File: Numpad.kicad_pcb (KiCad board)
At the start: 2 copper layers, 119.9 x 104.8 mm, 50 parts, among them SW1 SW_Push, U1 ATmega32U4-AU, Y1 16MHz

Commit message: Commit all files before starting from scratch
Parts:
- C1, C2, C3, C4, C5, C6, C7, D1, D10, D11, D12, D13, D14, D15, D16, D17, D2, D3, D4, D5, D6, D7, D8, D9, F1, R1, R2, R3, R4, SW1, U1, USB1, Y1: moved to B.Cu
- moved SW1 66.5 mm to (68.3, 43.3), turned to 180 degrees
- moved R1 56.4 mm to (75.2, 43.3), turned to 180 degrees
- moved C5 44.0 mm to (80.8, 38.9), turned to 180 degrees
- moved F1 39.1 mm to (79.2, 34.5)
- moved C6 38.2 mm to (80.8, 44.2)
- moved C7 34.9 mm to (94.7, 35.6), turned to 0 degrees
- moved R3 31.2 mm to (79.7, 29.9)
- moved U1 30.1 mm to (90.2, 43.4), turned to 270 degrees
- moved C4 29.1 mm to (95.2, 53.8), turned to 0 degrees
- moved USB1 28.3 mm to (81.3, 20.8)
- moved C3 28.0 mm to (98.8, 34.0)
- moved R2 26.6 mm to (82.1, 29.9)
- moved R4 24.3 mm to (86.4, 52.3)
- moved Y1 21.1 mm to (102.9, 42.4), turned to 270 degrees
- moved C2 18.6 mm to (102.9, 38.9), turned to 180 degrees
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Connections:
- net Net-(R2-Pad1) renamed /USB_D+
- net Net-(R3-Pad1) renamed /USB_D-
- USB1 pad 5: Net-(USB1-Pad5) -> VCC
- USB1 pad 6: VCC -> Net-(USB1-Pad6)
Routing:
- net COL0: track 0.00 -> 169.8 mm, vias 0 -> 2
- net COL2: track 0.00 -> 115.8 mm, vias 0 -> 1
- net COL1: track 0.00 -> 114.5 mm, vias 0 -> 1
- net ROW3: track 0.00 -> 106.1 mm, vias 0 -> 2
- net ROW4: track 0.00 -> 102.2 mm, vias 0 -> 2
- net ROW0: track 0.00 -> 82.8 mm, vias 0 -> 6
- net COL3: track 0.00 -> 82.6 mm
- net ROW2: track 0.00 -> 72.6 mm, vias 0 -> 2
- net +5V: track 0.00 -> 68.7 mm
- net ROW1: track 0.00 -> 59.5 mm
- net Net-(R1-Pad2): track 0.00 -> 26.9 mm, vias 0 -> 2
- net /USB_D-: track 0.00 -> 11.6 mm
- net Net-(C2-Pad1): track 0.00 -> 11.6 mm
- net /USB_D+: track 0.00 -> 11.6 mm
- net Net-(C1-Pad2): track 0.00 -> 9.34 mm
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- added copper zone on B.Cu, net GND
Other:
- board size 119.9 x 104.8 mm -> 88.9 x 104.8 mm
- net class Power added: clearance 0.2, trace_width 0.4, via_dia 0.8, via_drill 0.4

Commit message: Restart project
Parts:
- removed C7: 1uF, Capacitor_SMD:C_1206_3216Metric
- removed D14, D15, D16, D17, D4, D5, D6, D7, D8, D9: D_Small, Diode_SMD:D_SOD-123
- removed MX14, MX17, MX4, MX5, MX6, MX7, MX9: MX-NoLED, MX_Alps_Hybrid:MX-1U-NoLED
- removed MX15, MX8: MX-NoLED, MX_Alps_Hybrid:MX-2U-ReversedStabilizers-Vertical-NoLED
- removed MX16: MX-NoLED, MX_Alps_Hybrid:MX-2U-ReversedStabilizers-NoLED
- added D0: D_Small_ALT, Diode_SMD:D_SOD-123, B.Cu at (94.6, 58.3)
- added D20: D_Small_ALT, Diode_SMD:D_SOD-123, B.Cu at (94.6, 96.4)
- added D21: D_Small_ALT, Diode_SMD:D_SOD-123, B.Cu at (113.7, 96.4)
- added D22: D_Small_ALT, Diode_SMD:D_SOD-123, B.Cu at (132.7, 96.4)
- added D30: D_Small_ALT, Diode_SMD:D_SOD-123, B.Cu at (94.6, 115.4)
- added D31: D_Small_ALT, Diode_SMD:D_SOD-123, B.Cu at (113.7, 115.4)
- added D32: D_Small_ALT, Diode_SMD:D_SOD-123, B.Cu at (132.7, 115.4)
- added D33: D_Small_ALT, Diode_SMD:D_SOD-123, B.Cu at (138.4, 117.1)
- added D40: D_Small_ALT, Diode_SMD:D_SOD-123, B.Cu at (104.1, 121.0)
- added D42: D_Small_ALT, Diode_SMD:D_SOD-123, B.Cu at (132.7, 121.0)
- added MX0: MX-NoLED, MX_Only:MXOnly-1U-NoLED, F.Cu at (92.1, 54.0)
- added MX20: MX-NoLED, MX_Only:MXOnly-1U-NoLED, F.Cu at (92.1, 92.1)
- added MX21: MX-NoLED, MX_Only:MXOnly-1U-NoLED, F.Cu at (111.1, 92.1)
- added MX22: MX-NoLED, MX_Only:MXOnly-1U-NoLED, F.Cu at (130.2, 92.1)
- added MX30: MX-NoLED, MX_Only:MXOnly-1U-NoLED, F.Cu at (92.1, 111.1)
- added MX31: MX-NoLED, MX_Only:MXOnly-1U-NoLED, F.Cu at (111.1, 111.1)
- added MX32: MX-NoLED, MX_Only:MXOnly-1U-NoLED, F.Cu at (130.2, 111.1)
- added MX33: MX-NoLED, MX_Only:MXOnly-2U-ReversedStabilizers-NoLED, F.Cu at (149.2, 120.7)
- added MX40: MX-NoLED, MX_Only:MXOnly-2U-ReversedStabilizers-NoLED, F.Cu at (101.6, 130.2)
- added MX42: MX-NoLED, MX_Only:MXOnly-1U-NoLED, F.Cu at (130.2, 130.2)
- added R5: 22R, Resistor_SMD:R_0402_1005Metric, B.Cu at (103.5, 58.9)
- added R6: 10k, Resistor_SMD:R_0402_1005Metric, B.Cu at (101.3, 67.6)
- added U2: ATmega32U2-MU, Package_DFN_QFN:QFN-32-1EP_5x5mm_P0.5mm_EP3.1x3.1mm, B.Cu at (101.6, 63.5)
- C1, C2: value 22pF -> 100nF; footprint Capacitor_SMD:C_1206_3216Metric -> Capacitor_SMD:C_0402_1005Metric
- C3: value 0.1uF -> 10uF; footprint Capacitor_SMD:C_1206_3216Metric -> Capacitor_SMD:C_0603_1608Metric
- C4, C5: value 0.1uF -> 22pF; footprint Capacitor_SMD:C_1206_3216Metric -> Capacitor_SMD:C_0402_1005Metric
- C6: value 10uF -> 1uF; footprint Capacitor_SMD:C_1206_3216Metric -> Capacitor_SMD:C_0402_1005Metric
- D1, D10, D11, D12, D13, D2, D3: value D_Small -> D_Small_ALT
- F1: footprint Fuse:Fuse_1206_3216Metric -> Fuse:Fuse_0603_1608Metric
- MX1, MX10, MX11, MX12, MX2, MX3: footprint MX_Alps_Hybrid:MX-1U-NoLED -> MX_Only:MXOnly-1U-NoLED
- MX13: footprint MX_Alps_Hybrid:MX-1U-NoLED -> MX_Only:MXOnly-2U-ReversedStabilizers-NoLED
- R1: value 10k -> 5.1k; footprint Resistor_SMD:R_0805_2012Metric -> Resistor_SMD:R_0402_1005Metric
- R2: value 22 -> 5.1k; footprint Resistor_SMD:R_0805_2012Metric -> Resistor_SMD:R_0402_1005Metric
- R3: value 22 -> 10k; footprint Resistor_SMD:R_0805_2012Metric -> Resistor_SMD:R_0402_1005Metric
- R4: value 10k -> 22R; footprint Resistor_SMD:R_0805_2012Metric -> Resistor_SMD:R_0402_1005Metric
- SW1: footprint random-keyboard-parts:SKQG-1155865 -> Switches:TACTILE_SWITCH_SMD_5.2MM
- U1: value ATmega32U4-AU -> USBLC6-2SC6; footprint Package_QFP:TQFP-44_10x10mm_P0.8mm -> Package_TO_SOT_SMD:SOT-23-6
- USB1: value Molex-0548190589 -> HRO-TYPE-C-31-M-12; footprint random-keyboard-parts:Molex-0548190589 -> Type-C:HRO-TYPE-C-31-M-12
- moved MX12 98.4 mm to (130.2, 73.0)
- moved D12 97.9 mm to (132.7, 77.3)
- moved MX13 97.2 mm to (149.2, 82.5), turned to 90 degrees
- moved D13 84.4 mm to (138.4, 79.0), turned to 0 degrees
- moved D1 81.0 mm to (115.3, 56.9), turned to 180 degrees
- moved MX2 80.5 mm to (130.2, 54.0)
- moved MX1 80.5 mm to (111.1, 54.0)
- moved MX3 80.5 mm to (149.2, 54.0)
- moved D3 79.8 mm to (151.8, 58.3)
- moved D2 79.4 mm to (132.7, 58.3)
- moved MX10 39.7 mm to (92.1, 73.0)
- moved MX11 39.7 mm to (111.1, 73.0)
- moved C5 39.6 mm to (110.3, 65.3)
- moved D11 39.1 mm to (113.7, 77.3)
- moved D10 39.1 mm to (94.6, 77.3)
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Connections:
- C1 pad 1: GND -> +5V
- C1 pad 2: Net-(C1-Pad2) -> GND
- C2 pad 1: Net-(C2-Pad1) -> +5V
- C4 pad 1: +5V -> Net-(C4-Pad1)
- C5 pad 1: +5V -> Net-(C5-Pad1)
- C6 pad 1: +5V -> Net-(C6-Pad1)
- D10 pad 1: ROW2 -> ROW1
- D11 pad 1: ROW2 -> ROW1
- D12 pad 1: ROW3 -> ROW1
- D13 pad 1: ROW3 -> ROW1
- MX1 pad 1: COL0 -> COL1
- MX10 pad 1: COL1 -> COL0
- MX11 pad 1: COL2 -> COL1
- MX12 pad 1: COL0 -> COL2
- MX13 pad 1: COL1 -> COL3
- MX2 pad 1: COL1 -> COL2
- MX3 pad 1: COL2 -> COL3
- R1 pad 1: +5V -> Net-(R1-Pad1)
- R1 pad 2: Net-(R1-Pad2) -> GND
- R2 pad 1: /USB_D+ -> Net-(R2-Pad1)
- R2 pad 2: D+ -> GND
- R3 pad 1: /USB_D- -> +5V
- R3 pad 2: D- -> Net-(R3-Pad2)
- R4 pad 1: GND -> /MCU_D+
- R4 pad 2: Net-(R4-Pad2) -> D+
- SW1 pad 2: Net-(R1-Pad2) -> Net-(R3-Pad2)
- U1 pad 1: Net-(U1-Pad1) -> D-
- U1 pad 2: +5V -> GND
- U1 pad 3: /USB_D- -> D+
- U1 pad 4: /USB_D+ -> USB_D+
- U1 pad 5: GND -> +5V
- U1 pad 6: Net-(C7-Pad1) -> USB_D-
- USB1 pad 2: Net-(USB1-Pad2) -> VCC
- USB1 pad 3: D+ -> Net-(USB1-Pad3)
- USB1 pad 4: D- -> Net-(R2-Pad1)
- USB1 pad 5: VCC -> USB_D-
- USB1 pad 6: Net-(USB1-Pad6) -> USB_D+
- Y1 pad 1: Net-(C2-Pad1) -> Net-(C4-Pad1)
- Y1 pad 3: Net-(C1-Pad2) -> Net-(C5-Pad1)
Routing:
- net COL0: track 169.8 -> 94.5 mm, vias 2 -> 0
- net COL3: track 82.6 -> 132.5 mm
- net +5V: track 68.7 -> 35.7 mm, vias 0 -> 2
- net COL1: track 114.5 -> 82.5 mm
- net Net-(R1-Pad2): track 26.9 -> 0.00 mm, vias 2 -> 0
- net GND: track 7.21 -> 26.0 mm, vias 0 -> 23
- net ROW0: track 82.8 -> 64.0 mm, vias 6 -> 2
- net ROW4: track 102.2 -> 85.0 mm
- net COL2: track 115.8 -> 102.2 mm, vias 1 -> 0
- net ROW3: track 106.1 -> 93.4 mm
- net /USB_D-: track 11.6 -> 0.00 mm
- net Net-(C2-Pad1): track 11.6 -> 0.00 mm
- net /USB_D+: track 11.6 -> 0.00 mm
- net USB_D+: track 0.00 -> 10.4 mm
- net USB_D-: track 0.00 -> 9.97 mm, vias 0 -> 2
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- added copper zone on B.Cu, net +5V
- added copper zone on F.Cu, net GND
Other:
- board size 88.9 x 104.8 mm -> 81.3 x 100.3 mm
- net class Default: clearance 0.2 -> 0.127; trace_width 0.25 -> 0.127; via_dia 0.8 -> 0.6; via_drill 0.4 -> 0.3
- net class Power: clearance 0.2 -> 0.127; trace_width 0.4 -> 0.254; via_dia 0.8 -> 0.6; via_drill 0.4 -> 0.3
- rule trace_clearance: 0.2 -> 0.127
- rule trace_min: 0.2 -> 0.127
- rule via_min_size: 0.4 -> 0.2
- board text added: "*"
- board text added: "+"
- board text added: "-"
- board text added: "."
- board text added: "/"
- board text added: "0"
- board text added: "1"
- board text added: "2"
- board text added: "3"
- board text added: "4"
- board text added: "5"
- board text added: "6"
- board text added: "7"
- board text added: "8"
- board text added: "9"
- board text added: "Enter"
- board text added: "Numpad v1 Designed by Aaron Lucas and Oliver Martin"
- board text added: "num lk"

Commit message: Complete PCB v1
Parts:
- removed MX0, MX1: MX-NoLED, MX_Only:MXOnly-1U-NoLED
- added C7: 100nF, Capacitor_SMD:C_0603_1608Metric, B.Cu at (91.9, 64.9)
- added D1: D_Small, Diode_SMD:D_SOD-123, B.Cu at (94.0, 57.8)
- added J1: AVR-ISP-6, Connector_PinHeader_2.54mm:PinHeader_2x03_P2.54mm_Vertical, B.Cu at (84.3, 78.2)
- added MX00: MX-NoLED, MX_Only:MXOnly-1U-NoLED, F.Cu at (92.1, 54.0)
- added MX01: MX-NoLED, MX_Only:MXOnly-1U-NoLED, F.Cu at (111.1, 54.0)
- added R7: 330R, Resistor_SMD:R_0603_1608Metric, B.Cu at (92.9, 62.2)
- added REF**: MountingHole_2.2mm_M2_Pad, MountingHole:MountingHole_2.2mm_M2_Pad, F.Cu at (152.5, 101.6)
- added REF**: MountingHole_2.2mm_M2_Pad, MountingHole:MountingHole_2.2mm_M2_Pad, F.Cu at (83.9, 130.2)
- added REF**: MountingHole_2.2mm_M2_Pad, MountingHole:MountingHole_2.2mm_M2_Pad, F.Cu at (139.7, 54.0)
- added REF**: MountingHole_2.2mm_M2_Pad, MountingHole:MountingHole_2.2mm_M2_Pad, F.Cu at (99.1, 82.5)
- C1, C2, C4, C5, C6: footprint Capacitor_SMD:C_0402_1005Metric -> Capacitor_SMD:C_0603_1608Metric
- R1, R2, R3, R4, R5, R6: footprint Resistor_SMD:R_0402_1005Metric -> Resistor_SMD:R_0603_1608Metric
- U2: value ATmega32U2-MU -> ATmega32U2-AU; footprint Package_DFN_QFN:QFN-32-1EP_5x5mm_P0.5mm_EP3.1x3.1mm -> Package_QFP:TQFP-32_7x7mm_P0.8mm
- USB1: value HRO-TYPE-C-31-M-12 -> DX07S016JA1R1500; footprint Type-C:HRO-TYPE-C-31-M-12 -> DX07S016JA1R1500:JAE_DX07S016JA1R1500
- moved D00 5.78 mm to (88.9, 57.4)
- moved USB1 5.08 mm to (101.6, 47.0)
- moved R6 4.54 mm to (101.2, 72.1)
- moved F1 4.35 mm to (99.1, 51.1)
- moved C4 3.42 mm to (113.7, 59.8)
- moved C5 3.36 mm to (113.7, 64.8)
- moved C2 3.32 mm to (108.7, 64.8)
- moved Y1 3.25 mm to (113.6, 62.3)
- moved R3 3.13 mm to (95.6, 61.3)
- moved C3 2.21 mm to (106.8, 57.4)
- moved C1 2.17 mm to (106.8, 58.9)
- moved C6 1.72 mm to (99.7, 58.1)
- moved R1 1.68 mm to (104.2, 49.9)
- moved U1 1.57 mm to (103.1, 54.3)
- moved U2 1.53 mm to (101.7, 65.0)
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- renumbered D0 to D00, D1 to D01, D2 to D02, D3 to D03, MX2 to MX02, MX3 to MX03
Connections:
- R3 pad 2: Net-(R3-Pad2) -> RESET
- SW1 pad 2: Net-(R3-Pad2) -> Net-(R7-Pad2)
- U2 pad 10: COL2 -> ROW3
- U2 pad 11: COL1 -> ROW2
- U2 pad 12: Net-(U2-Pad12) -> ROW1
- U2 pad 14: ROW4 -> Net-(U2-Pad14)
- U2 pad 15: ROW3 -> SCK
- U2 pad 16: ROW2 -> MOSI
- U2 pad 17: ROW1 -> MISO
- U2 pad 24: Net-(R3-Pad2) -> RESET
- U2 pad 6: Net-(U2-Pad6) -> COL3
- U2 pad 7: Net-(U2-Pad7) -> COL2
- U2 pad 8: Net-(U2-Pad8) -> COL1
- U2 pad 9: COL3 -> ROW4
- USB1 pad 10: Net-(R1-Pad1) -> Net-(USB1-Pad10)
- USB1 pad 3: Net-(USB1-Pad3) -> Net-(R2-Pad1)
- USB1 pad 4: Net-(R2-Pad1) -> Net-(USB1-Pad4)
- USB1 pad 7: USB_D- -> USB_D+
- USB1 pad 8: USB_D+ -> USB_D-
- USB1 pad 9: Net-(USB1-Pad9) -> Net-(R1-Pad1)
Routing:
- net RESET: track 0.00 -> 29.0 mm, vias 0 -> 3
- net MISO: track 0.00 -> 23.4 mm
- net MOSI: track 0.00 -> 23.3 mm
- net SCK: track 0.00 -> 19.4 mm
- net +5V: track 35.7 -> 49.6 mm, vias 2 -> 0
- net Net-(R3-Pad2): track 8.88 -> 0.00 mm
- net ROW4: track 85.0 -> 78.9 mm
- net ROW1: track 57.9 -> 52.0 mm
- net GND: track 26.0 -> 31.0 mm, vias 23 -> 19
- net ROW0: track 64.0 -> 68.9 mm, vias 2 -> 4
- net COL2: track 102.2 -> 98.0 mm
- net VCC: track 12.8 -> 8.67 mm
- net ROW2: track 70.9 -> 66.9 mm
- net USB_D+: track 10.4 -> 6.44 mm
- net COL1: track 82.5 -> 79.0 mm
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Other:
- board text removed: "/"
- board text removed: "num lk"

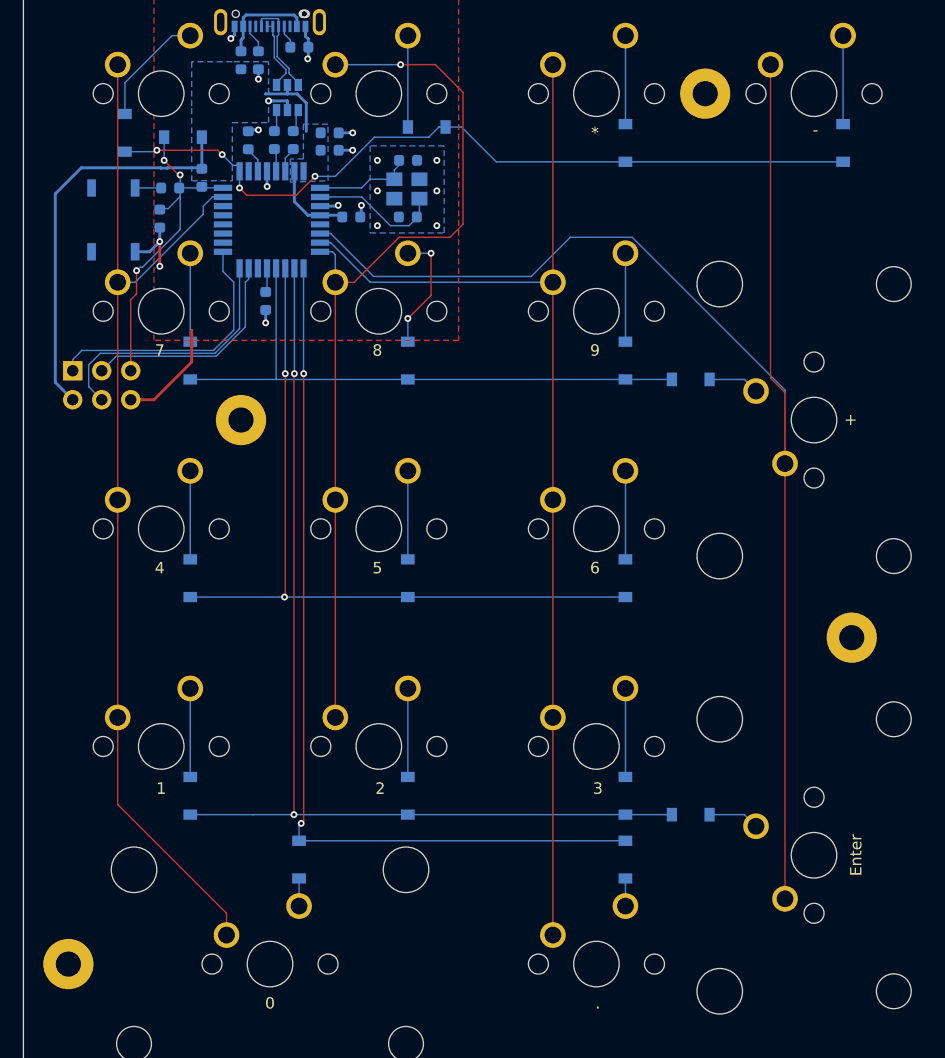
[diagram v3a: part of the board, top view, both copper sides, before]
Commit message: Fix issues with reset button and bootloader mode
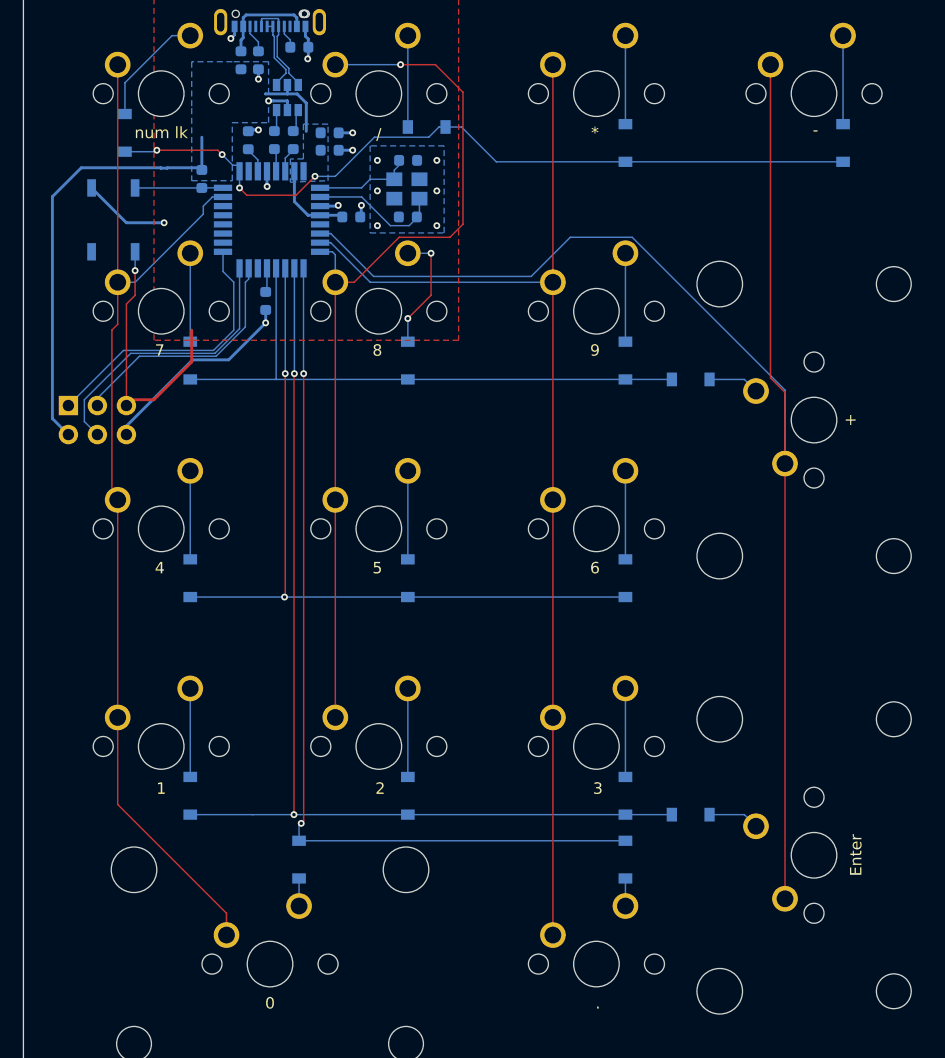
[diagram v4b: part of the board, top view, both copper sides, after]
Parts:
- removed C7: 100nF, Capacitor_SMD:C_0603_1608Metric
- removed the D1 at (94.0, 57.8)
- removed J1: AVR-ISP-6, Connector_PinHeader_2.54mm:PinHeader_2x03_P2.54mm_Vertical
- removed R7: 330R, Resistor_SMD:R_0603_1608Metric
- removed REF** (x4): MountingHole_2.2mm_M2_Pad, MountingHole:MountingHole_2.2mm_M2_Pad
- removed SW1: SW_Push, Switches:TACTILE_SWITCH_SMD_5.2MM
- added ICSP: AVR-ISP-6, Connector_PinHeader_2.54mm:PinHeader_2x03_P2.54mm_Vertical, B.Cu at (83.9, 81.3)
- added RESET: SW_SPST, Button_Switch_SMD:TACTILE_SWITCH_SPST_SMD_5.2MM, B.Cu at (87.9, 65.0)
- moved R3 0.10 mm to (95.6, 61.4)
- renumbered D00 to D0, D01 to D1, D02 to D2, D03 to D3, MX00 to MX0, MX01 to MX1, MX02 to MX2, MX03 to MX3
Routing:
- net GND: track 31.0 -> 40.0 mm, vias 19 -> 18
- net +5V: track 49.6 -> 52.7 mm
- net Net-(R7-Pad2): track 2.20 -> 0.00 mm
- net SCK: track 19.4 -> 21.4 mm
- net RESET: track 29.0 -> 30.8 mm, vias 3 -> 1
- net MOSI: track 23.3 -> 25.0 mm
- net MISO: track 23.4 -> 24.5 mm
- net COL0: track 92.9 -> 93.9 mm
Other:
- board text added: "/"
- board text added: "GND"
- board text added: "MISO"
- board text added: "MOSI"
- board text added: "Numpad v1.1 Designed by Aaron Lucas and Oliver Martin"
- board text added: "RST"
- board text added: "SCK"
- board text added: "VCC"
- board text added: "num lk"
- board text removed: "Numpad v1 Designed by Aaron Lucas and Oliver Martin"
